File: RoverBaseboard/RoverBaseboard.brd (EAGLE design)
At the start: 87 x 61.6 mm, 58 parts, among them IC1 7805, IC3 3.3V, U2 microSD

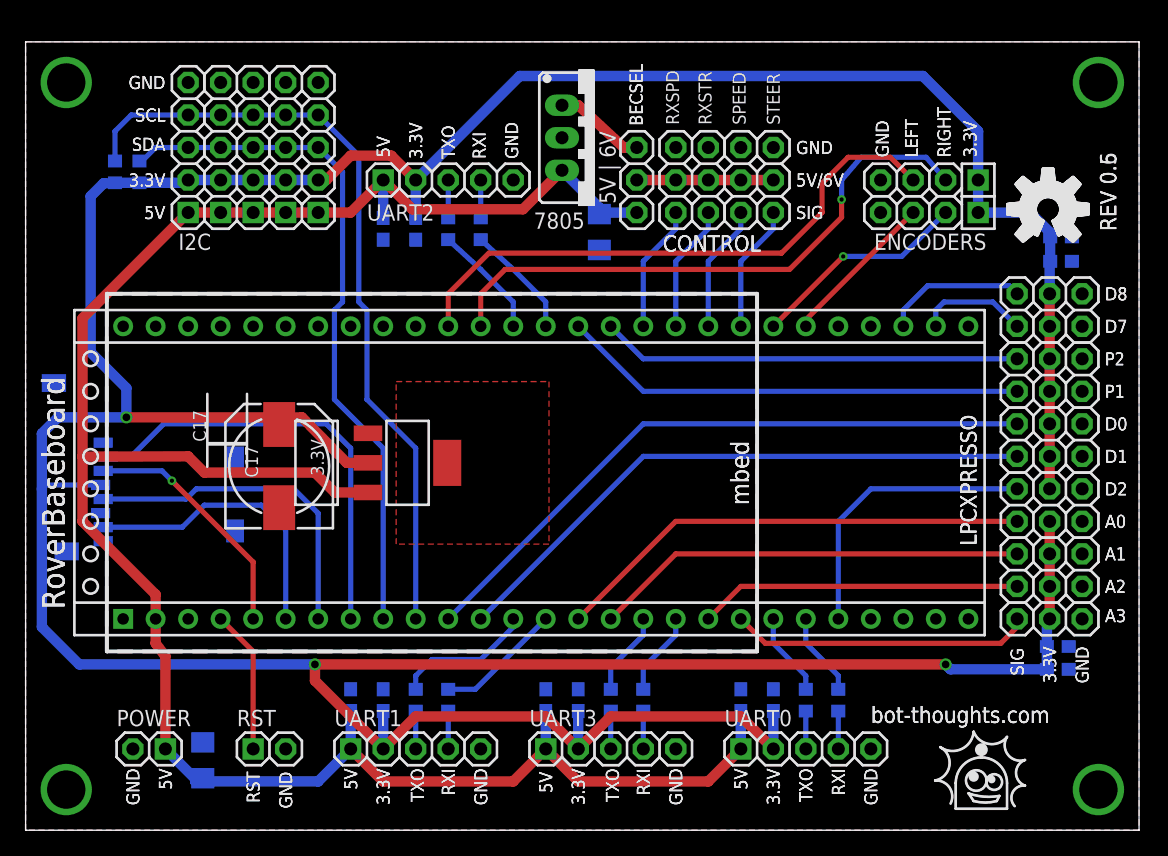
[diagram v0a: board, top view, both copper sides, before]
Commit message: Bugfix to supply--3.3V regulator now feeds LPCXpresso. Minor tweaks. Powering analog ports more directly. Rerouted power. Moved power pins to align to 0.1" spacing. Heat sink now connected to 3V3 out.
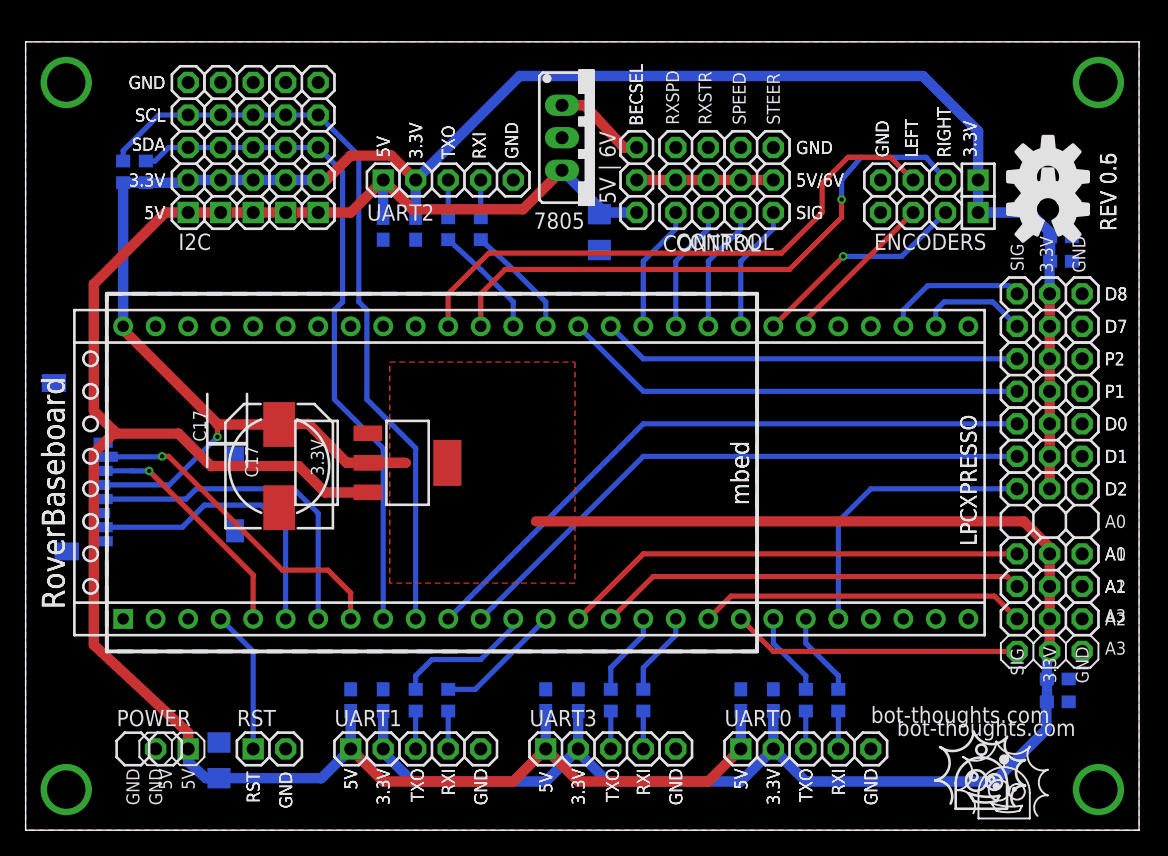
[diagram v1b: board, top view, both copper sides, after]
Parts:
- moved C6 2.54 mm to (80.6, 11.8)
- moved C7 2.54 mm to (80.6, 10.0)
- moved JP19 2.54 mm to (80.0, 14.0)
- moved JP16 2.54 mm to (80.0, 21.6)
- moved JP17 2.54 mm to (80.0, 19.1)
- moved JP18 2.54 mm to (80.0, 16.5)
- moved JP3 1.78 mm to (11.4, 6.35)
- moved C2 1.27 mm to (15.1, 5.46)
- moved R6 0.63 mm to (7.62, 51.4)
- moved R5 0.51 mm to (9.40, 51.4)
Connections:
- removed net SINK: IC3.4
- net +3V3: now also IC3.4, U$1.J6-28
- net +5V: no longer U$1.J6-2
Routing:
- net +3V3: track 322.6 -> 282.1 mm, vias 3 -> 1
- net !CS1: track 34.1 -> 25.4 mm, vias 0 -> 1
- net +5V: track 176.0 -> 174.1 mm
- net SCL: track 61.3 -> 59.7 mm
- net A0: track 37.4 -> 36.4 mm
- net A3: track 23.5 -> 22.6 mm
- net MOSI1: track 19.1 -> 18.5 mm
- net SDA: track 53.9 -> 53.4 mm
- added copper zone on layer 1, net +3V3
- removed copper zone on layer 1, net SINK

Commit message: Change to LDO regulator, added port labels for digital, analog, encoders, change cap values.
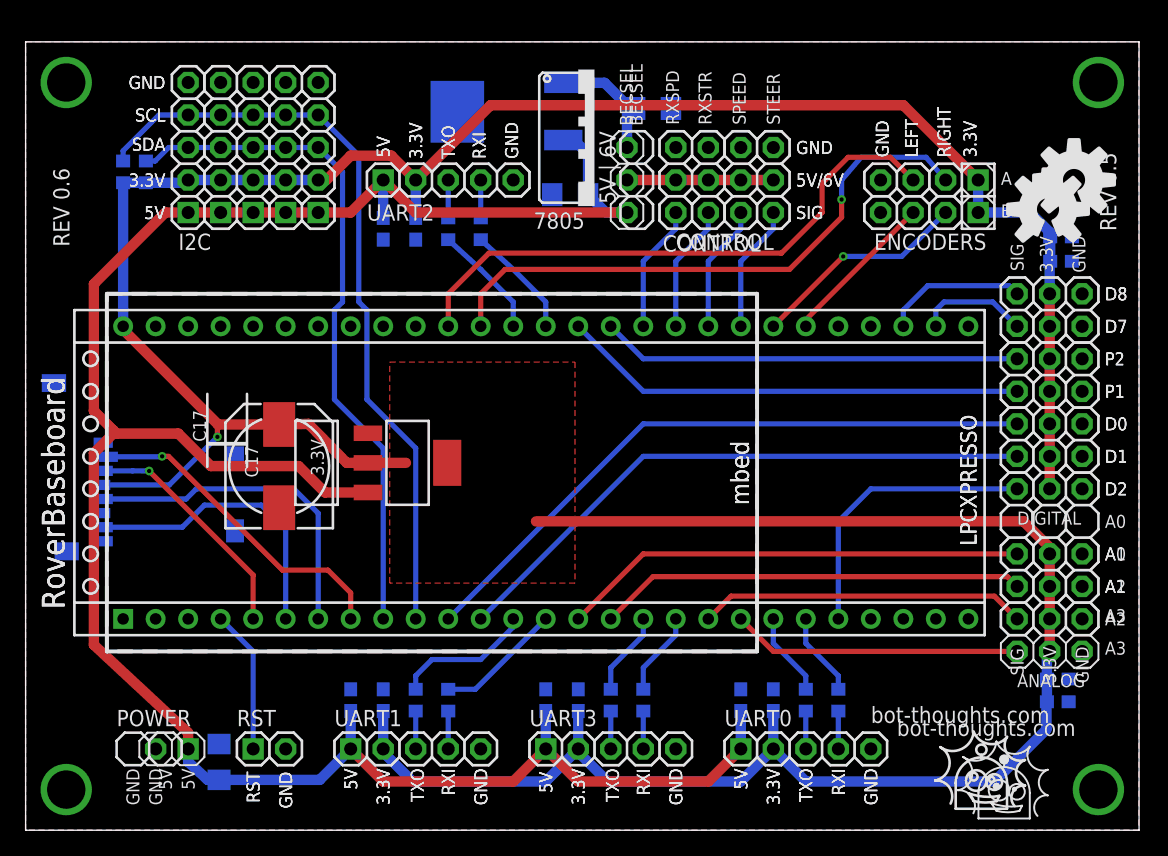
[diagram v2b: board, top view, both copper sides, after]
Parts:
- removed IC1: 7805, v-reg-3:78XXS
- added C1: 106, rcl:C1206
- added U1: LD29150DT50R, bt_regulator:DPAK
- C10, C11, C12, C13, C14, C15, C2, C3, C4, C6, C8, C9: value 10 -> 106
- C17: value 100 -> 33uF
- C5, C7: value 0.1 -> 104
- moved C2 52.0 mm to (42.5, 49.7), turned to 0 degrees
- moved C3 51.0 mm to (15.1, 5.33), turned to 90 degrees
- moved BECSEL 0.76 mm to (47.0, 50.8)
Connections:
- net +5V: now also U1.3; no longer IC1.OUT
- net GND: now also C1.2, U1.4; no longer IC1.GND
- net N$3: now also C1.1, U1.1; no longer IC1.IN
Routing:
- net +5V: track 174.1 -> 179.7 mm
- net +3V3: track 282.1 -> 278.0 mm
- net N$3: track 7.29 -> 9.64 mm
- net BEC: track 10.7 -> 11.4 mm
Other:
- board text added: "A"
- board text added: "ANALOG"
- board text added: "B"
- board text added: "DIGITAL"

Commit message: Renamed VBEC net
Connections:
- net N$3 renamed VBEC
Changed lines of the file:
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@@
 <wire x1="58.42" y1="13.97" x2="55.88" y2="16.51" width="0.4064" layer="1"/>
 </signal>
-<signal name="N$3">
+<signal name="VBEC">
 <contactref element="BECSEL" pad="1"/>
 <contactref element="U1" pad="1"/>

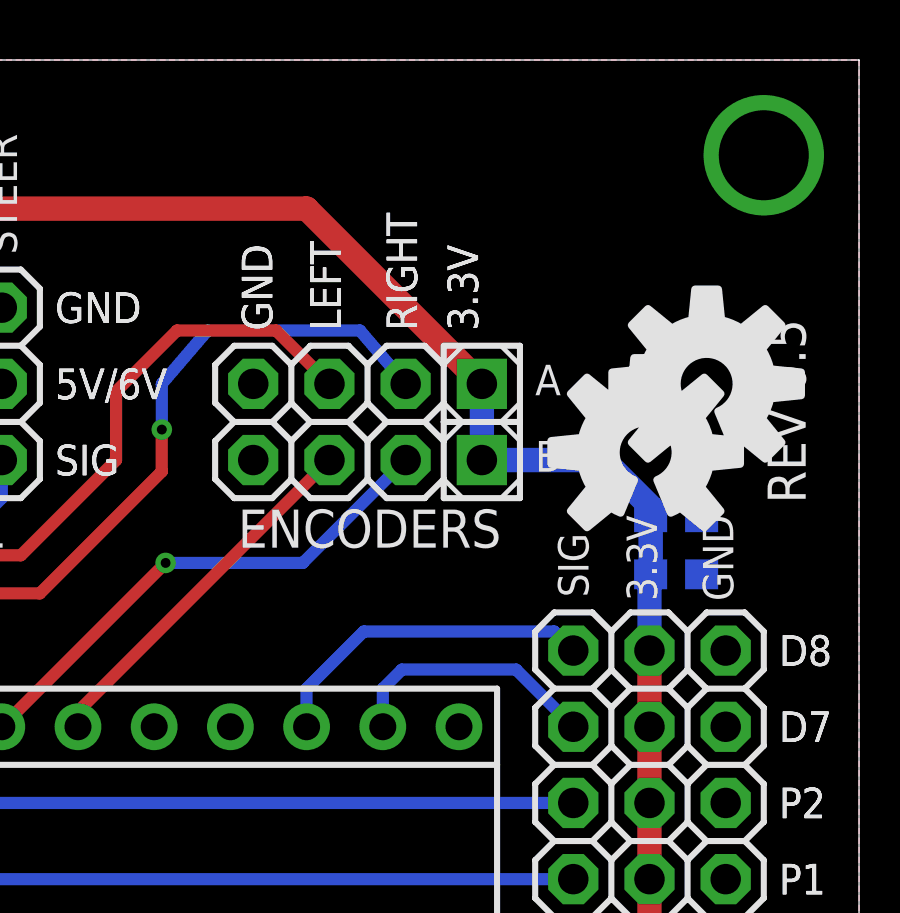
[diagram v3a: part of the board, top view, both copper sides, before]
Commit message: Added ISP pushbutton and pullup
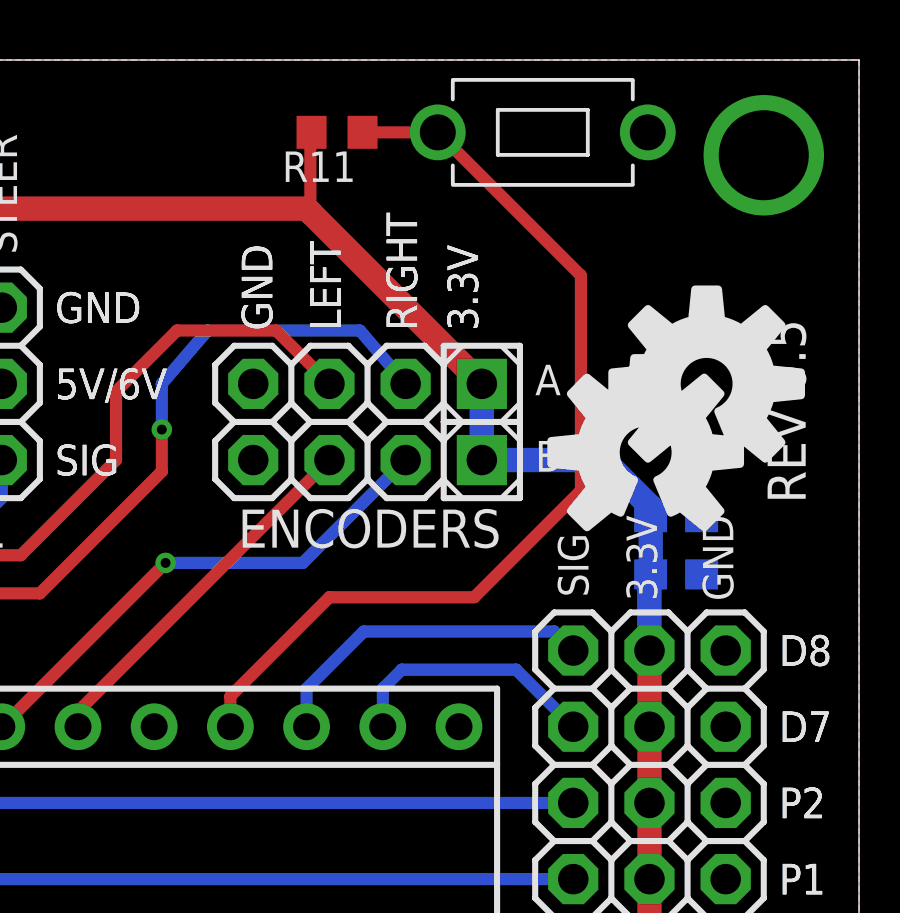
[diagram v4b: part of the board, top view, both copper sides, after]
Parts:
- added R11: 10K, rcl:R0603
- added S1: ISP, bt_electromech:6MMTACTILE_RECT
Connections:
- net !ISP: now also R11.1, S1.P$2
- net +3V3: now also R11.2
- net GND: now also S1.P$1
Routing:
- net !ISP: track 0.00 -> 32.0 mm
- net +3V3: track 278.0 -> 280.7 mm
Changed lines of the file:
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@@
 <attribute name="NAME" x="50.038" y="57.912" size="1.27" layer="26" rot="MR0"/>
+</element>
+<element name="S1" library="bt_electromech" package="6MMTACTILE_RECT" value="ISP" x="76.454" y="59.182" smashed="yes" rot="R180">
+<attribute name="VALUE" x="79.502" y="56.896" size="1.27" layer="27" rot="R180"/>
+</element>
+<element name="R11" library="rcl" package="R0603" value="10K" x="69.596" y="59.182" smashed="yes" rot="R180">
+<attribute name="OC_NEWARK" value="98K2621" x="69.596" y="59.182" size="1.778" layer="27" rot="R180" display="off"/>
+<attribute name="MPN" value="WCR0805-220RFI" x="69.596" y="59.182" size="1.778" layer="27" rot="R180" display="off"/>
+<attribute name="MF" value="" x="69.596" y="59.182" size="1.778" layer="27" rot="R180" display="off"/>
+<attribute name="NAME" x="70.231" y="58.547" size="1.016" layer="25" rot="R180"/>
 </element>
 </elements>
@@
 <contactref element="U1" pad="4"/>
 <contactref element="C1" pad="2"/>
+<contactref element="S1" pad="P$1"/>
 </signal>
 <signal name="MOSI1">
@@
 <wire x1="79.756" y1="7.874" x2="79.756" y2="9.994" width="0.8128" layer="16"/>
 <wire x1="79.756" y1="9.994" x2="79.795" y2="10.033" width="0.8128" layer="16"/>
-<wire x1="74.422" y1="50.8" x2="68.58" y2="56.642" width="0.8128" layer="1"/>
+<wire x1="74.422" y1="50.8" x2="68.707" y2="56.515" width="0.8128" layer="1"/>
+<wire x1="68.707" y1="56.515" x2="68.58" y2="56.642" width="0.8128" layer="1"/>
 <wire x1="68.58" y1="56.642" x2="36.322" y2="56.642" width="0.8128" layer="1"/>
 <wire x1="36.322" y1="56.642" x2="30.48" y2="50.8" width="0.8128" layer="1"/>
+<contactref element="R11" pad="2"/>
+<wire x1="68.746" y1="59.182" x2="68.707" y2="59.182" width="0.4064" layer="1"/>
+<wire x1="68.707" y1="59.182" x2="68.707" y2="56.515" width="0.4064" layer="1"/>
 </signal>
 <signal name="SDA">
@@
 <signal name="!ISP">
 <contactref element="U$1" pad="J6-51"/>
+<contactref element="R11" pad="1"/>
+<contactref element="S1" pad="P$2"/>
+<wire x1="72.954" y1="59.182" x2="70.446" y2="59.182" width="0.4064" layer="1"/>
+<wire x1="66.04" y1="39.37" x2="66.04" y2="40.386" width="0.4064" layer="1"/>
+<wire x1="66.04" y1="40.386" x2="69.342" y2="43.688" width="0.4064" layer="1"/>
+<wire x1="69.342" y1="43.688" x2="74.168" y2="43.688" width="0.4064" layer="1"/>
+<wire x1="74.168" y1="43.688" x2="77.724" y2="47.244" width="0.4064" layer="1"/>
+<wire x1="77.724" y1="47.244" x2="77.724" y2="54.412" width="0.4064" layer="1"/>
+<wire x1="77.724" y1="54.412" x2="72.954" y2="59.182" width="0.4064" layer="1"/>
 </signal>
 <signal name="ENC0">

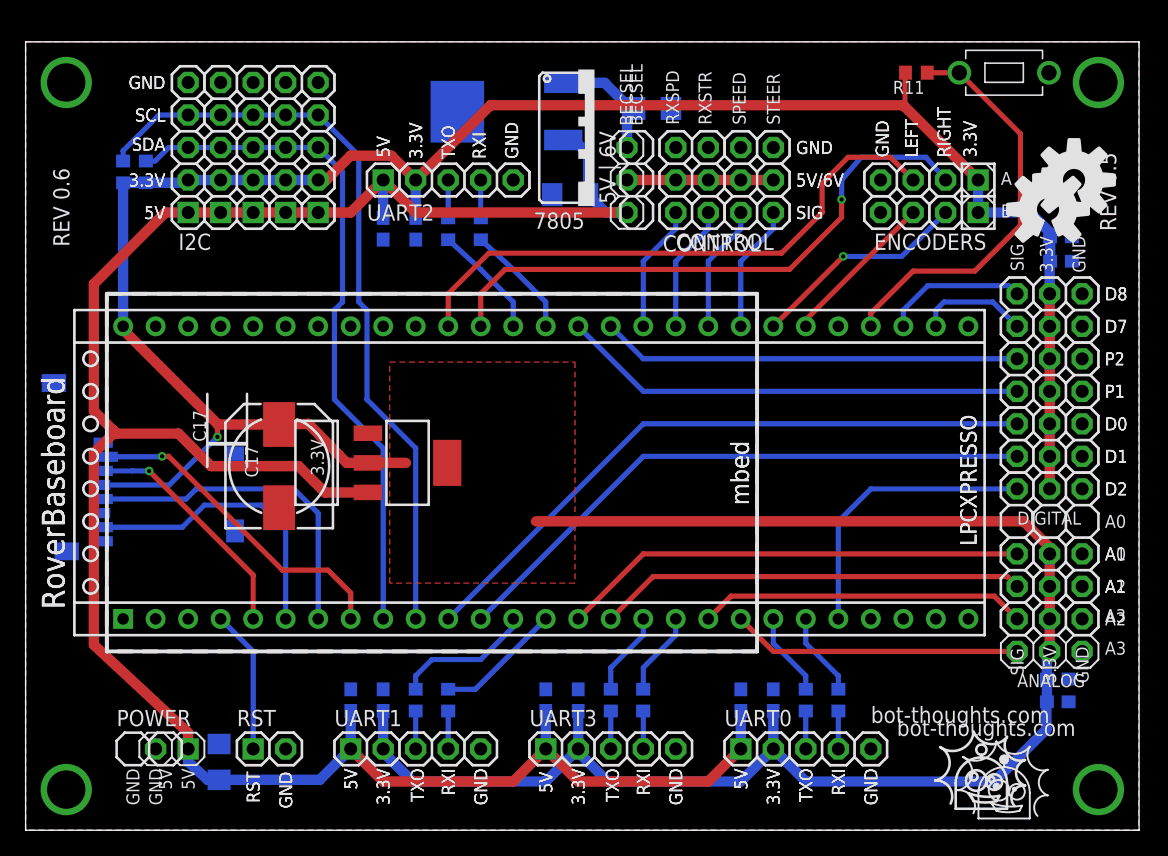
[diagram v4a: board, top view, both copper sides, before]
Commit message: Added ISP pin headers, revised power supply selection layout, added pin header for selecting external 5VIN in addition to selections for 5V or 6V BEC. Renumbered capacitors. Verified cap voltages, etc.
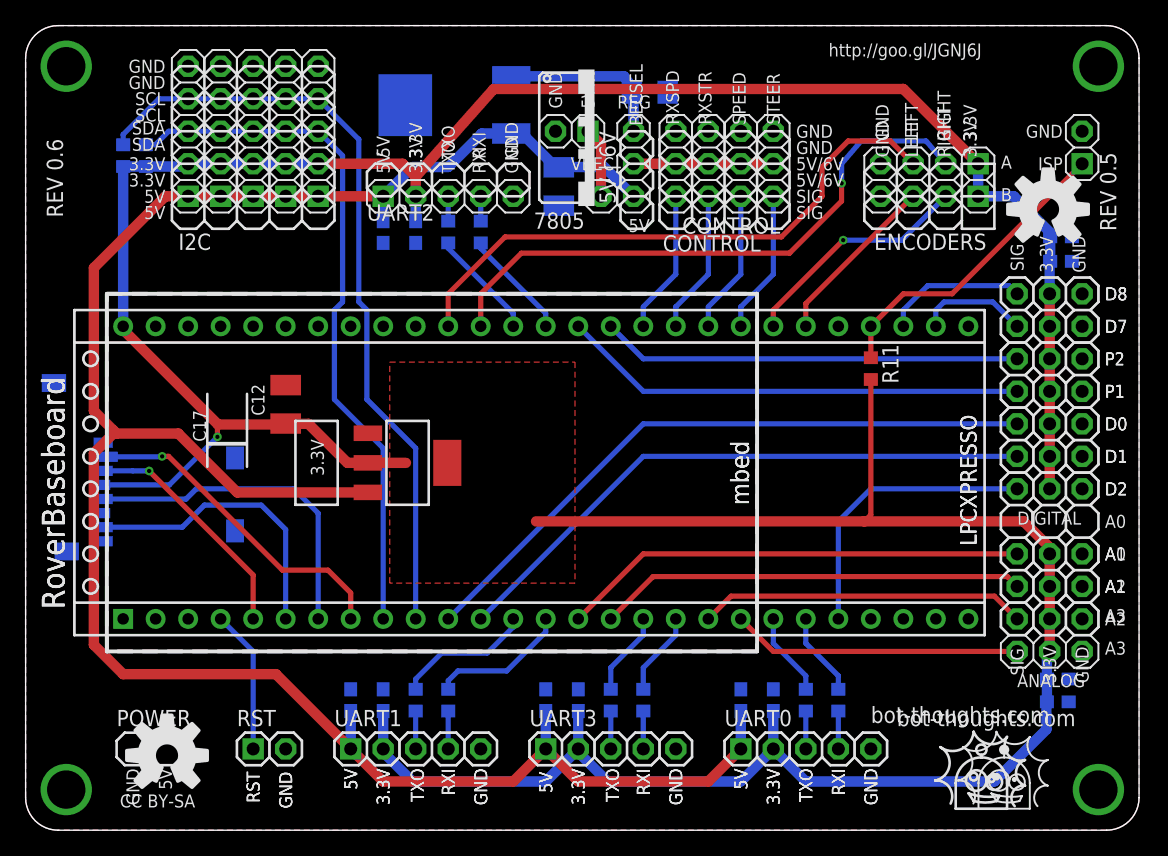
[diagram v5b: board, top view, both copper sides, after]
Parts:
- removed BECSEL: 5V | 6V, pinhead-2:1X03-S
- removed C1, C2, C3: 106, rcl:C1206
- removed C15: 106, rcl:C0603
- removed C17: 33uF, rcl:140CLH-0810
- removed S1: ISP, bt_electromech:6MMTACTILE_RECT
- added BEC: BYP | REG, pinhead-2:1X03-S
- added C40, C41, C46\, C47: 106, rcl:C0603
- added JP12: 5VIN, pinhead-2:1X01-S
- added JP30: ISP, pinhead-2:1X02-S
- C10: device rcl:C0603 -> rcl:C1206
- C11, C12: value 106 -> 33uF; device rcl:C0603 -> rcl:SMC_B
- JP3: value POWER -> PWR
- moved JP3 57.5 mm to (42.7, 54.6)
- moved C10 48.0 mm to (48.8, 57.7), turned to 180 degrees
- moved C12 44.6 mm to (20.3, 33.3), flipped to the top
- moved R11 23.4 mm to (66.0, 36.1), turned to 270 degrees
- moved C11 14.1 mm to (41.7, 50.3)
- moved U1 4.10 mm to (34.3, 56.6)
- moved JP15 1.27 mm to (70.6, 52.1)
- moved JP2 1.27 mm to (70.6, 49.5)
- moved JP5 1.27 mm to (50.8, 52.1)
- moved JP6 1.27 mm to (53.3, 52.1)
- moved JP8 1.27 mm to (55.9, 52.1)
- moved JP9 1.27 mm to (58.4, 52.1)
- moved JP21 1.27 mm to (33.0, 49.5)
- moved JP23 1.27 mm to (12.7, 54.6)
- moved JP24 1.27 mm to (15.2, 54.6)
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- renumbered C13 to C43, C14 to C45, C4 to C30, C5 to C31, C6 to C20, C7 to C21, C8 to C42, C9 to C44
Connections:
- removed net VBEC: BECSEL.1, C1.1, U1.1
- new net 5VIN: JP12.1, JP3.1
- new net 6-7V: BEC.1, C10.1, U1.1
- net !ISP: now also JP30.1; no longer S1.P$2
- net +3V3: now also C12.+, C41.1, C47.1; no longer C12.1, C15.1, C17.+
- net +5V: now also BEC.3, C11.+, C40.1, C46\.1; no longer BECSEL.3, C10.1, C11.1, C2.1, C3.1, JP3.1
- net BEC: now also BEC.2; no longer BECSEL.2
- net GND: now also C11.-, C12.-, C40.2, C41.2, C46\.2, C47.2, JP30.2; no longer C1.2, C11.2, C12.2, C15.2, C17.-, C2.2, C3.2, S1.P$1
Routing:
- net 6-7V: track 0.00 -> 13.6 mm
- net +3V3: track 280.7 -> 291.2 mm
- net VBEC: track 9.64 -> 0.00 mm
- net +5V: track 179.7 -> 170.1 mm
- net !ISP: track 32.0 -> 24.2 mm
- net 5VIN: track 0.00 -> 5.50 mm
- net STEER: track 9.94 -> 11.2 mm
- net SPEED: track 9.94 -> 11.2 mm
- net RXSTR: track 9.94 -> 11.2 mm
- net RXSPD: track 9.94 -> 11.2 mm
- net ENC3: track 12.4 -> 13.6 mm
- net ENC2: track 17.1 -> 18.4 mm
- net SDA: track 53.4 -> 54.6 mm
- net SCL: track 59.7 -> 61.0 mm
- net N$17: track 2.96 -> 1.94 mm
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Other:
- board size 87 x 61.6 mm -> 87 x 62.9 mm
- board text added: "5VIN"
- board text added: "CC BY-SA"
- board text added: "ISP"
- board text added: "REG"
- board text added: "VBEC"
- board text added: "http://goo.gl/JGNJ6J"

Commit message: Added documentation to schematic
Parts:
- BEC: value BYP | REG -> REG | BYP | 5VIN
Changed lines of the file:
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@@
 <attribute name="NAME" x="18.669" y="32.385" size="1.016" layer="25" ratio="10" rot="R90"/>
 </element>
-<element name="BEC" library="pinhead-2" package="1X03-S" value="BYP | REG" x="47.498" y="52.07" smashed="yes" rot="R270"/>
+<element name="BEC" library="pinhead-2" package="1X03-S" value="REG | BYP | 5VIN" x="47.498" y="52.07" smashed="yes" rot="R270"/>
 <element name="U1" library="bt_regulator" package="DPAK" value="LD29150DT50R" x="34.29" y="56.642" smashed="yes" rot="MR270">
 <attribute name="NAME" x="33.528" y="59.182" size="1.27" layer="26" ratio="10" rot="MR270"/>
